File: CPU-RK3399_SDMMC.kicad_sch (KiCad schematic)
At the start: 1 part, among them U1 RK3399

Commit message: design CPU-RK3399 eMMC Controller
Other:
- company: (none) -> TickLab
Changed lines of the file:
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@@
 	(paper "A4")
 	(title_block
-		(date "2026-01-09")
+		(date "2026-01-14")
 		(rev "1.0.0")
+		(company "TickLab")
 	)
 	(no_connect

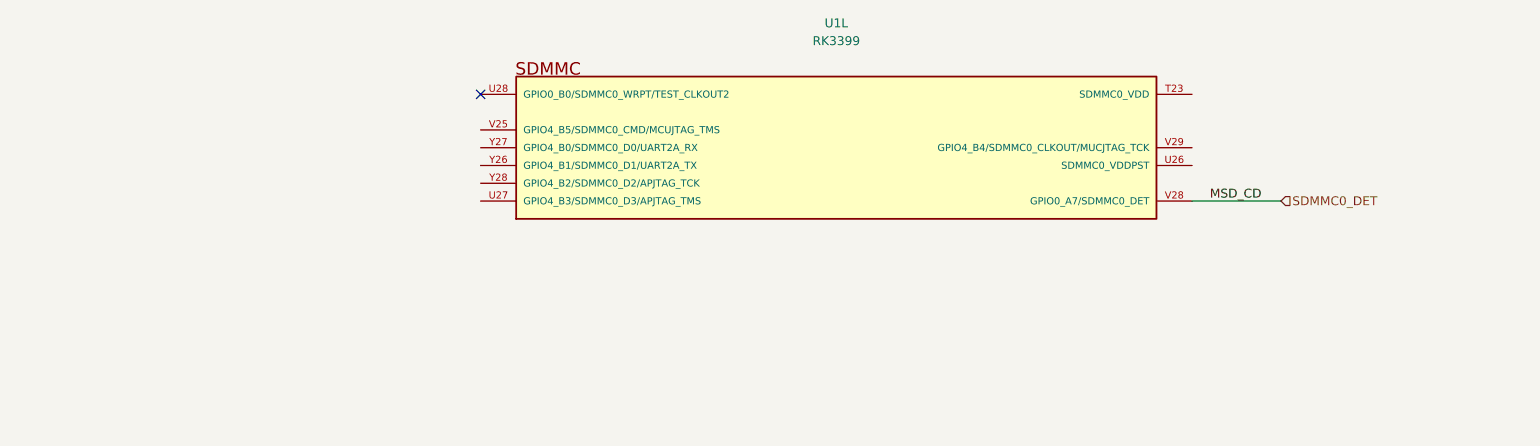
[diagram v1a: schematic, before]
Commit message: design CPU-RK3399 SDMMC
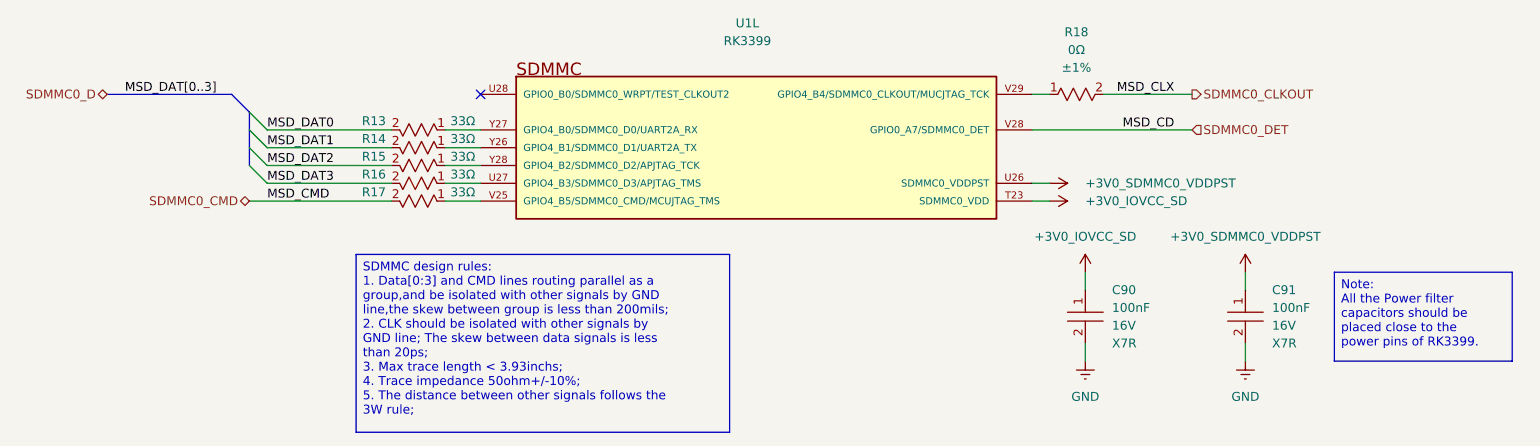
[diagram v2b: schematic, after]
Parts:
- added C90, C91: ~, footprints:CAPC1005X50N, symbol component_library:Capacitors/CL05B104KO5NNNC
- added R13, R14, R15, R16, R17: ~, footprints:RESC1005X35N, symbol component_library:Resistors/0402WGF330JTCE
- added R18: ~, footprints:RESC1005X35N, symbol component_library:Resistors/0402WGF0000TCE
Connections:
- net +3V0_IOVCC_SD: now reaches U1.T23 (SDMMC0_VDD)
- net +3V0_IOVCC_SD: now also C90.1
- net +3V0_SDMMC0_VDDPST: now reaches U1.U26 (SDMMC0_VDDPST)
- net +3V0_SDMMC0_VDDPST: now also C91.1
- net at U1.U27 (GPIO4_B3/SDMMC0_D3/APJTAG_TMS): now also R16.1
- net at U1.V25 (GPIO4_B5/SDMMC0_CMD/MCUJTAG_TMS): now also R17.1
- net at U1.V29 (GPIO4_B4/SDMMC0_CLKOUT/MUCJTAG_TCK): now also R18.1
- net at U1.Y26 (GPIO4_B1/SDMMC0_D1/UART2A_TX): now also R14.1
- net at U1.Y27 (GPIO4_B0/SDMMC0_D0/UART2A_RX): now also R13.1
- net at U1.Y28 (GPIO4_B2/SDMMC0_D2/APJTAG_TCK): now also R15.1
- new net GND: C90.2, C91.2
- new net MSD_DAT0: R13.2
- new net MSD_DAT1: R14.2
- new net MSD_DAT2: R15.2
- new net MSD_DAT3: R16.2
- new net SDMMC0_CLKOUT: R18.2
- new net SDMMC0_CMD: R17.2
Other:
- title: (none) -> CPU-RK3399 SDMMC Controller
- moved on the sheet: U1L

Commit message: design USB
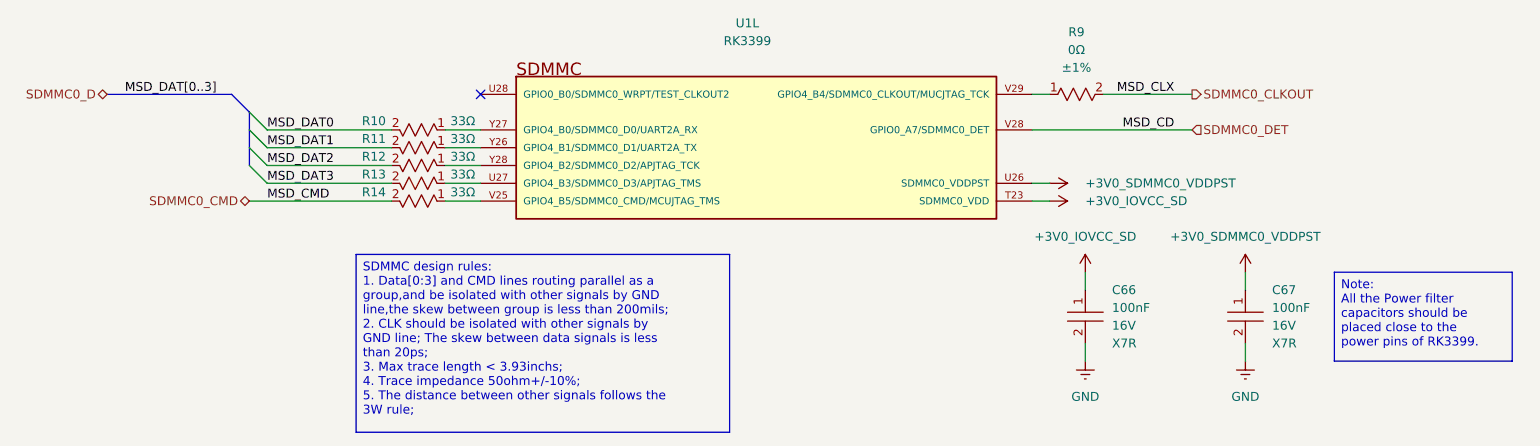
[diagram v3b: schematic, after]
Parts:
- renumbered C90 to C66, C91 to C67, R13 to R10, R14 to R11, R15 to R12, R16 to R13, R17 to R14, R18 to R9
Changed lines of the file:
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@@
 		(on_board yes)
 		(dnp no)
-		(property "Reference" "#PWR075"
+		(property "Reference" "#PWR047"
 			(at 179.07 111.76 0)
 			(effects
@@
 			(project "VESA-SBC3399"
 				(path "/ebc9dc57-8b05-484a-a5cd-c53b1efc71d3/a7299b18-4123-434b-8c69-0b9524fffa12/a2f1a77f-77be-4fa6-bc18-df703764e02b"
-					(reference "#PWR075")
+					(reference "#PWR047")
 					(unit 1)
 				)
@@
 		(on_board yes)
 		(dnp no)
-		(property "Reference" "R15"
+		(property "Reference" "R12"
 			(at 86.36 105.41 0)
 			(effects
@@
 			(project "VESA-SBC3399"
 				(path "/ebc9dc57-8b05-484a-a5cd-c53b1efc71d3/a7299b18-4123-434b-8c69-0b9524fffa12/a2f1a77f-77be-4fa6-bc18-df703764e02b"
-					(reference "R15")
+					(reference "R12")
 					(unit 1)
 				)
@@
 		(on_board yes)
 		(dnp no)
-		(property "Reference" "#PWR074"
+		(property "Reference" "#PWR046"
 			(at 179.07 109.22 0)
 			(effects
@@
 			(project "VESA-SBC3399"
 				(path "/ebc9dc57-8b05-484a-a5cd-c53b1efc71d3/a7299b18-4123-434b-8c69-0b9524fffa12/a2f1a77f-77be-4fa6-bc18-df703764e02b"
-					(reference "#PWR074")
+					(reference "#PWR046")
 					(unit 1)
 				)
@@
 		(on_board yes)
 		(dnp no)
-		(property "Reference" "C91"
+		(property "Reference" "C67"
 			(at 214.63 124.4599 0)
 			(effects
@@
 			(project "VESA-SBC3399"
 				(path "/ebc9dc57-8b05-484a-a5cd-c53b1efc71d3/a7299b18-4123-434b-8c69-0b9524fffa12/a2f1a77f-77be-4fa6-bc18-df703764e02b"
-					(reference "C91")
+					(reference "C67")
 					(unit 1)
 				)
@@
 		(on_board yes)
 		(dnp no)
-		(property "Reference" "R13"
+		(property "Reference" "R10"
 			(at 86.36 100.33 0)
 			(effects
@@
 			(project "VESA-SBC3399"
 				(path "/ebc9dc57-8b05-484a-a5cd-c53b1efc71d3/a7299b18-4123-434b-8c69-0b9524fffa12/a2f1a77f-77be-4fa6-bc18-df703764e02b"
-					(reference "R13")
+					(reference "R10")
 					(unit 1)
 				)
@@
 		(on_board yes)
 		(dnp no)
-		(property "Reference" "#PWR076"
+		(property "Reference" "#PWR048"
 			(at 187.96 125.73 0)
 			(effects
@@
 			(project "VESA-SBC3399"
 				(path "/ebc9dc57-8b05-484a-a5cd-c53b1efc71d3/a7299b18-4123-434b-8c69-0b9524fffa12/a2f1a77f-77be-4fa6-bc18-df703764e02b"
-					(reference "#PWR076")
+					(reference "#PWR048")
 					(unit 1)
 				)
@@
 		(on_board yes)
 		(dnp no)
-		(property "Reference" "R14"
+		(property "Reference" "R11"
 			(at 86.36 102.87 0)
 			(effects
@@
 			(project "VESA-SBC3399"
 				(path "/ebc9dc57-8b05-484a-a5cd-c53b1efc71d3/a7299b18-4123-434b-8c69-0b9524fffa12/a2f1a77f-77be-4fa6-bc18-df703764e02b"
-					(reference "R14")
+					(reference "R11")
 					(unit 1)
 				)
@@
 		(dnp no)
 		(fields_autoplaced yes)
-		(property "Reference" "#PWR072"
+		(property "Reference" "#PWR050"
 			(at 187.96 140.97 0)
 			(effects
@@
 			(project "VESA-SBC3399"
 				(path "/ebc9dc57-8b05-484a-a5cd-c53b1efc71d3/a7299b18-4123-434b-8c69-0b9524fffa12/a2f1a77f-77be-4fa6-bc18-df703764e02b"
-					(reference "#PWR072")
+					(reference "#PWR050")
 					(unit 1)
 				)
@@
 		(dnp no)
 		(fields_autoplaced yes)
-		(property "Reference" "R18"
+		(property "Reference" "R9"
 			(at 186.69 87.63 0)
 			(effects
@@
 			(project "VESA-SBC3399"
 				(path "/ebc9dc57-8b05-484a-a5cd-c53b1efc71d3/a7299b18-4123-434b-8c69-0b9524fffa12/a2f1a77f-77be-4fa6-bc18-df703764e02b"
-					(reference "R18")
+					(reference "R9")
 					(unit 1)
 				)
@@
 		(on_board yes)
 		(dnp no)
-		(property "Reference" "C90"
+		(property "Reference" "C66"
 			(at 191.77 124.4599 0)
 			(effects
@@
 			(project "VESA-SBC3399"
 				(path "/ebc9dc57-8b05-484a-a5cd-c53b1efc71d3/a7299b18-4123-434b-8c69-0b9524fffa12/a2f1a77f-77be-4fa6-bc18-df703764e02b"
-					(reference "C90")
+					(reference "C66")
 					(unit 1)
 				)
@@
 		(on_board yes)
 		(dnp no)
-		(property "Reference" "R17"
+		(property "Reference" "R14"
 			(at 86.36 110.49 0)
 			(effects
@@
 			(project "VESA-SBC3399"
 				(path "/ebc9dc57-8b05-484a-a5cd-c53b1efc71d3/a7299b18-4123-434b-8c69-0b9524fffa12/a2f1a77f-77be-4fa6-bc18-df703764e02b"
-					(reference "R17")
+					(reference "R14")
 					(unit 1)
 				)
@@
 		(on_board yes)
 		(dnp no)
-		(property "Reference" "R16"
+		(property "Reference" "R13"
 			(at 86.36 107.95 0)
 			(effects
@@
 			(project "VESA-SBC3399"
 				(path "/ebc9dc57-8b05-484a-a5cd-c53b1efc71d3/a7299b18-4123-434b-8c69-0b9524fffa12/a2f1a77f-77be-4fa6-bc18-df703764e02b"
-					(reference "R16")
+					(reference "R13")
 					(unit 1)
 				)
@@
 		(on_board yes)
 		(dnp no)
-		(property "Reference" "#PWR077"
+		(property "Reference" "#PWR049"
 			(at 210.82 125.73 0)
 			(effects
@@
 			(project "VESA-SBC3399"
 				(path "/ebc9dc57-8b05-484a-a5cd-c53b1efc71d3/a7299b18-4123-434b-8c69-0b9524fffa12/a2f1a77f-77be-4fa6-bc18-df703764e02b"
-					(reference "#PWR077")
+					(reference "#PWR049")
 					(unit 1)
 				)
@@
 		(dnp no)
 		(fields_autoplaced yes)
-		(property "Reference" "#PWR073"
+		(property "Reference" "#PWR051"
 			(at 210.82 140.97 0)
 			(effects
@@
 			(project "VESA-SBC3399"
 				(path "/ebc9dc57-8b05-484a-a5cd-c53b1efc71d3/a7299b18-4123-434b-8c69-0b9524fffa12/a2f1a77f-77be-4fa6-bc18-df703764e02b"
-					(reference "#PWR073")
+					(reference "#PWR051")
 					(unit 1)
 				)

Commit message: update design power
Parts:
- renumbered C66 to C121, C67 to C122, R9 to R32, R10 to R33, R11 to R34, R12 to R35, R13 to R36, R14 to R37, U1 to U2
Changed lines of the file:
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@@
 		(on_board yes)
 		(dnp no)
-		(property "Reference" "#PWR047"
+		(property "Reference" "#PWR0134"
 			(at 179.07 111.76 0)
 			(effects
@@
 			(project "VESA-SBC3399"
 				(path "/ebc9dc57-8b05-484a-a5cd-c53b1efc71d3/a7299b18-4123-434b-8c69-0b9524fffa12/a2f1a77f-77be-4fa6-bc18-df703764e02b"
-					(reference "#PWR047")
+					(reference "#PWR0134")
 					(unit 1)
 				)
@@
 		(on_board yes)
 		(dnp no)
-		(property "Reference" "R12"
+		(property "Reference" "R35"
 			(at 86.36 105.41 0)
 			(effects
@@
 			(project "VESA-SBC3399"
 				(path "/ebc9dc57-8b05-484a-a5cd-c53b1efc71d3/a7299b18-4123-434b-8c69-0b9524fffa12/a2f1a77f-77be-4fa6-bc18-df703764e02b"
-					(reference "R12")
+					(reference "R35")
 					(unit 1)
 				)
@@
 		(on_board yes)
 		(dnp no)
-		(property "Reference" "#PWR046"
+		(property "Reference" "#PWR0133"
 			(at 179.07 109.22 0)
 			(effects
@@
 			(project "VESA-SBC3399"
 				(path "/ebc9dc57-8b05-484a-a5cd-c53b1efc71d3/a7299b18-4123-434b-8c69-0b9524fffa12/a2f1a77f-77be-4fa6-bc18-df703764e02b"
-					(reference "#PWR046")
+					(reference "#PWR0133")
 					(unit 1)
 				)
@@
 		(on_board yes)
 		(dnp no)
-		(property "Reference" "C67"
+		(property "Reference" "C122"
 			(at 214.63 124.4599 0)
 			(effects
@@
 			(project "VESA-SBC3399"
 				(path "/ebc9dc57-8b05-484a-a5cd-c53b1efc71d3/a7299b18-4123-434b-8c69-0b9524fffa12/a2f1a77f-77be-4fa6-bc18-df703764e02b"
-					(reference "C67")
+					(reference "C122")
 					(unit 1)
 				)
@@
 		(on_board yes)
 		(dnp no)
-		(property "Reference" "R10"
+		(property "Reference" "R33"
 			(at 86.36 100.33 0)
 			(effects
@@
 			(project "VESA-SBC3399"
 				(path "/ebc9dc57-8b05-484a-a5cd-c53b1efc71d3/a7299b18-4123-434b-8c69-0b9524fffa12/a2f1a77f-77be-4fa6-bc18-df703764e02b"
-					(reference "R10")
+					(reference "R33")
 					(unit 1)
 				)
@@
 		(on_board yes)
 		(dnp no)
-		(property "Reference" "#PWR048"
+		(property "Reference" "#PWR0135"
 			(at 187.96 125.73 0)
 			(effects
@@
 			(project "VESA-SBC3399"
 				(path "/ebc9dc57-8b05-484a-a5cd-c53b1efc71d3/a7299b18-4123-434b-8c69-0b9524fffa12/a2f1a77f-77be-4fa6-bc18-df703764e02b"
-					(reference "#PWR048")
+					(reference "#PWR0135")
 					(unit 1)
 				)
@@
 		(on_board yes)
 		(dnp no)
-		(property "Reference" "R11"
+		(property "Reference" "R34"
 			(at 86.36 102.87 0)
 			(effects
@@
 			(project "VESA-SBC3399"
 				(path "/ebc9dc57-8b05-484a-a5cd-c53b1efc71d3/a7299b18-4123-434b-8c69-0b9524fffa12/a2f1a77f-77be-4fa6-bc18-df703764e02b"
-					(reference "R11")
+					(reference "R34")
 					(unit 1)
 				)
@@
 		(dnp no)
 		(fields_autoplaced yes)
-		(property "Reference" "#PWR050"
+		(property "Reference" "#PWR0137"
 			(at 187.96 140.97 0)
 			(effects
@@
 			(project "VESA-SBC3399"
 				(path "/ebc9dc57-8b05-484a-a5cd-c53b1efc71d3/a7299b18-4123-434b-8c69-0b9524fffa12/a2f1a77f-77be-4fa6-bc18-df703764e02b"
-					(reference "#PWR050")
+					(reference "#PWR0137")
 					(unit 1)
 				)
@@
 		(dnp no)
 		(fields_autoplaced yes)
-		(property "Reference" "R9"
+		(property "Reference" "R32"
 			(at 186.69 87.63 0)
 			(effects
@@
 			(project "VESA-SBC3399"
 				(path "/ebc9dc57-8b05-484a-a5cd-c53b1efc71d3/a7299b18-4123-434b-8c69-0b9524fffa12/a2f1a77f-77be-4fa6-bc18-df703764e02b"
-					(reference "R9")
+					(reference "R32")
 					(unit 1)
 				)
@@
 		(on_board yes)
 		(dnp no)
-		(property "Reference" "C66"
+		(property "Reference" "C121"
 			(at 191.77 124.4599 0)
 			(effects
@@
 			(project "VESA-SBC3399"
 				(path "/ebc9dc57-8b05-484a-a5cd-c53b1efc71d3/a7299b18-4123-434b-8c69-0b9524fffa12/a2f1a77f-77be-4fa6-bc18-df703764e02b"
-					(reference "C66")
+					(reference "C121")
 					(unit 1)
 				)
@@
 		(on_board yes)
 		(dnp no)
-		(property "Reference" "R14"
+		(property "Reference" "R37"
 			(at 86.36 110.49 0)
 			(effects
@@
 			(project "VESA-SBC3399"
 				(path "/ebc9dc57-8b05-484a-a5cd-c53b1efc71d3/a7299b18-4123-434b-8c69-0b9524fffa12/a2f1a77f-77be-4fa6-bc18-df703764e02b"
-					(reference "R14")
+					(reference "R37")
 					(unit 1)
 				)
@@
 		(on_board yes)
 		(dnp no)
-		(property "Reference" "R13"
+		(property "Reference" "R36"
 			(at 86.36 107.95 0)
 			(effects
@@
 			(project "VESA-SBC3399"
 				(path "/ebc9dc57-8b05-484a-a5cd-c53b1efc71d3/a7299b18-4123-434b-8c69-0b9524fffa12/a2f1a77f-77be-4fa6-bc18-df703764e02b"
-					(reference "R13")
+					(reference "R36")
 					(unit 1)
 				)
@@
 		(dnp no)
 		(fields_autoplaced yes)
-		(property "Reference" "U1"
+		(property "Reference" "U2"
 			(at 139.7 86.36 0)
 			(effects
@@
 			(project "VESA-SBC3399"
 				(path "/ebc9dc57-8b05-484a-a5cd-c53b1efc71d3/a7299b18-4123-434b-8c69-0b9524fffa12/a2f1a77f-77be-4fa6-bc18-df703764e02b"
-					(reference "U1")
+					(reference "U2")
 					(unit 12)
 				)
@@
 		(on_board yes)
 		(dnp no)
-		(property "Reference" "#PWR049"
+		(property "Reference" "#PWR0136"
 			(at 210.82 125.73 0)
 			(effects
@@
 			(project "VESA-SBC3399"
 				(path "/ebc9dc57-8b05-484a-a5cd-c53b1efc71d3/a7299b18-4123-434b-8c69-0b9524fffa12/a2f1a77f-77be-4fa6-bc18-df703764e02b"
-					(reference "#PWR049")
+					(reference "#PWR0136")
 					(unit 1)
 				)
@@
 		(dnp no)
 		(fields_autoplaced yes)
-		(property "Reference" "#PWR051"
+		(property "Reference" "#PWR0138"
 			(at 210.82 140.97 0)
 			(effects
@@
 			(project "VESA-SBC3399"
 				(path "/ebc9dc57-8b05-484a-a5cd-c53b1efc71d3/a7299b18-4123-434b-8c69-0b9524fffa12/a2f1a77f-77be-4fa6-bc18-df703764e02b"
-					(reference "#PWR051")
+					(reference "#PWR0138")
 					(unit 1)
 				)

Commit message: design DDR
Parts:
- renumbered C121 to C248, C122 to C249, R32 to R103, R33 to R104, R34 to R105, R35 to R106, R36 to R107, R37 to R108, U2 to U17
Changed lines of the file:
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@@
 		(on_board yes)
 		(dnp no)
-		(property "Reference" "#PWR0134"
+		(property "Reference" "#PWR0294"
 			(at 179.07 111.76 0)
 			(effects
@@
 			(project "VESA-SBC3399"
 				(path "/ebc9dc57-8b05-484a-a5cd-c53b1efc71d3/a7299b18-4123-434b-8c69-0b9524fffa12/a2f1a77f-77be-4fa6-bc18-df703764e02b"
-					(reference "#PWR0134")
+					(reference "#PWR0294")
 					(unit 1)
 				)
@@
 		(on_board yes)
 		(dnp no)
-		(property "Reference" "R35"
+		(property "Reference" "R106"
 			(at 86.36 105.41 0)
 			(effects
@@
 			(project "VESA-SBC3399"
 				(path "/ebc9dc57-8b05-484a-a5cd-c53b1efc71d3/a7299b18-4123-434b-8c69-0b9524fffa12/a2f1a77f-77be-4fa6-bc18-df703764e02b"
-					(reference "R35")
+					(reference "R106")
 					(unit 1)
 				)
@@
 		(on_board yes)
 		(dnp no)
-		(property "Reference" "#PWR0133"
+		(property "Reference" "#PWR0293"
 			(at 179.07 109.22 0)
 			(effects
@@
 			(project "VESA-SBC3399"
 				(path "/ebc9dc57-8b05-484a-a5cd-c53b1efc71d3/a7299b18-4123-434b-8c69-0b9524fffa12/a2f1a77f-77be-4fa6-bc18-df703764e02b"
-					(reference "#PWR0133")
+					(reference "#PWR0293")
 					(unit 1)
 				)
@@
 		(on_board yes)
 		(dnp no)
-		(property "Reference" "C122"
+		(property "Reference" "C249"
 			(at 214.63 124.4599 0)
 			(effects
@@
 			(project "VESA-SBC3399"
 				(path "/ebc9dc57-8b05-484a-a5cd-c53b1efc71d3/a7299b18-4123-434b-8c69-0b9524fffa12/a2f1a77f-77be-4fa6-bc18-df703764e02b"
-					(reference "C122")
+					(reference "C249")
 					(unit 1)
 				)
@@
 		(on_board yes)
 		(dnp no)
-		(property "Reference" "R33"
+		(property "Reference" "R104"
 			(at 86.36 100.33 0)
 			(effects
@@
 			(project "VESA-SBC3399"
 				(path "/ebc9dc57-8b05-484a-a5cd-c53b1efc71d3/a7299b18-4123-434b-8c69-0b9524fffa12/a2f1a77f-77be-4fa6-bc18-df703764e02b"
-					(reference "R33")
+					(reference "R104")
 					(unit 1)
 				)
@@
 		(on_board yes)
 		(dnp no)
-		(property "Reference" "#PWR0135"
+		(property "Reference" "#PWR0295"
 			(at 187.96 125.73 0)
 			(effects
@@
 			(project "VESA-SBC3399"
 				(path "/ebc9dc57-8b05-484a-a5cd-c53b1efc71d3/a7299b18-4123-434b-8c69-0b9524fffa12/a2f1a77f-77be-4fa6-bc18-df703764e02b"
-					(reference "#PWR0135")
+					(reference "#PWR0295")
 					(unit 1)
 				)
@@
 		(on_board yes)
 		(dnp no)
-		(property "Reference" "R34"
+		(property "Reference" "R105"
 			(at 86.36 102.87 0)
 			(effects
@@
 			(project "VESA-SBC3399"
 				(path "/ebc9dc57-8b05-484a-a5cd-c53b1efc71d3/a7299b18-4123-434b-8c69-0b9524fffa12/a2f1a77f-77be-4fa6-bc18-df703764e02b"
-					(reference "R34")
+					(reference "R105")
 					(unit 1)
 				)
@@
 		(dnp no)
 		(fields_autoplaced yes)
-		(property "Reference" "#PWR0137"
+		(property "Reference" "#PWR0297"
 			(at 187.96 140.97 0)
 			(effects
@@
 			(project "VESA-SBC3399"
 				(path "/ebc9dc57-8b05-484a-a5cd-c53b1efc71d3/a7299b18-4123-434b-8c69-0b9524fffa12/a2f1a77f-77be-4fa6-bc18-df703764e02b"
-					(reference "#PWR0137")
+					(reference "#PWR0297")
 					(unit 1)
 				)
@@
 		(dnp no)
 		(fields_autoplaced yes)
-		(property "Reference" "R32"
+		(property "Reference" "R103"
 			(at 186.69 87.63 0)
 			(effects
@@
 			(project "VESA-SBC3399"
 				(path "/ebc9dc57-8b05-484a-a5cd-c53b1efc71d3/a7299b18-4123-434b-8c69-0b9524fffa12/a2f1a77f-77be-4fa6-bc18-df703764e02b"
-					(reference "R32")
+					(reference "R103")
 					(unit 1)
 				)
@@
 		(on_board yes)
 		(dnp no)
-		(property "Reference" "C121"
+		(property "Reference" "C248"
 			(at 191.77 124.4599 0)
 			(effects
@@
 			(project "VESA-SBC3399"
 				(path "/ebc9dc57-8b05-484a-a5cd-c53b1efc71d3/a7299b18-4123-434b-8c69-0b9524fffa12/a2f1a77f-77be-4fa6-bc18-df703764e02b"
-					(reference "C121")
+					(reference "C248")
 					(unit 1)
 				)
@@
 		(on_board yes)
 		(dnp no)
-		(property "Reference" "R37"
+		(property "Reference" "R108"
 			(at 86.36 110.49 0)
 			(effects
@@
 			(project "VESA-SBC3399"
 				(path "/ebc9dc57-8b05-484a-a5cd-c53b1efc71d3/a7299b18-4123-434b-8c69-0b9524fffa12/a2f1a77f-77be-4fa6-bc18-df703764e02b"
-					(reference "R37")
+					(reference "R108")
 					(unit 1)
 				)
@@
 		(on_board yes)
 		(dnp no)
-		(property "Reference" "R36"
+		(property "Reference" "R107"
 			(at 86.36 107.95 0)
 			(effects
@@
 			(project "VESA-SBC3399"
 				(path "/ebc9dc57-8b05-484a-a5cd-c53b1efc71d3/a7299b18-4123-434b-8c69-0b9524fffa12/a2f1a77f-77be-4fa6-bc18-df703764e02b"
-					(reference "R36")
+					(reference "R107")
 					(unit 1)
 				)
@@
 		(dnp no)
 		(fields_autoplaced yes)
-		(property "Reference" "U2"
-			(at 139.7 86.36 0)
+		(property "Reference" "U17"
+			(at 140.97 86.36 0)
 			(effects
 				(font
@@
 		)
 		(property "Value" "RK3399"
-			(at 139.7 88.9 0)
+			(at 140.97 88.9 0)
 			(effects
 				(font
@@
 		)
 		(property "Footprint" "footprints:BGA828C65P31X31_2100X2100X161"
-			(at 157.48 111.76 0)
+			(at 139.7 111.76 0)
 			(effects
 				(font
@@
 			(project "VESA-SBC3399"
 				(path "/ebc9dc57-8b05-484a-a5cd-c53b1efc71d3/a7299b18-4123-434b-8c69-0b9524fffa12/a2f1a77f-77be-4fa6-bc18-df703764e02b"
-					(reference "U2")
+					(reference "U17")
 					(unit 12)
 				)
@@
 		(on_board yes)
 		(dnp no)
-		(property "Reference" "#PWR0136"
+		(property "Reference" "#PWR0296"
 			(at 210.82 125.73 0)
 			(effects
@@
 			(project "VESA-SBC3399"
 				(path "/ebc9dc57-8b05-484a-a5cd-c53b1efc71d3/a7299b18-4123-434b-8c69-0b9524fffa12/a2f1a77f-77be-4fa6-bc18-df703764e02b"
-					(reference "#PWR0136")
+					(reference "#PWR0296")
 					(unit 1)
 				)
@@
 		(dnp no)
 		(fields_autoplaced yes)
-		(property "Reference" "#PWR0138"
+		(property "Reference" "#PWR0298"
 			(at 210.82 140.97 0)
 			(effects
@@
 			(project "VESA-SBC3399"
 				(path "/ebc9dc57-8b05-484a-a5cd-c53b1efc71d3/a7299b18-4123-434b-8c69-0b9524fffa12/a2f1a77f-77be-4fa6-bc18-df703764e02b"
-					(reference "#PWR0138")
+					(reference "#PWR0298")
 					(unit 1)
 				)
